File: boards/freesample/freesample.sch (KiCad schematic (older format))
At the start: 5 parts, among them J1 SMA, J2 CONN_3_PWROUT

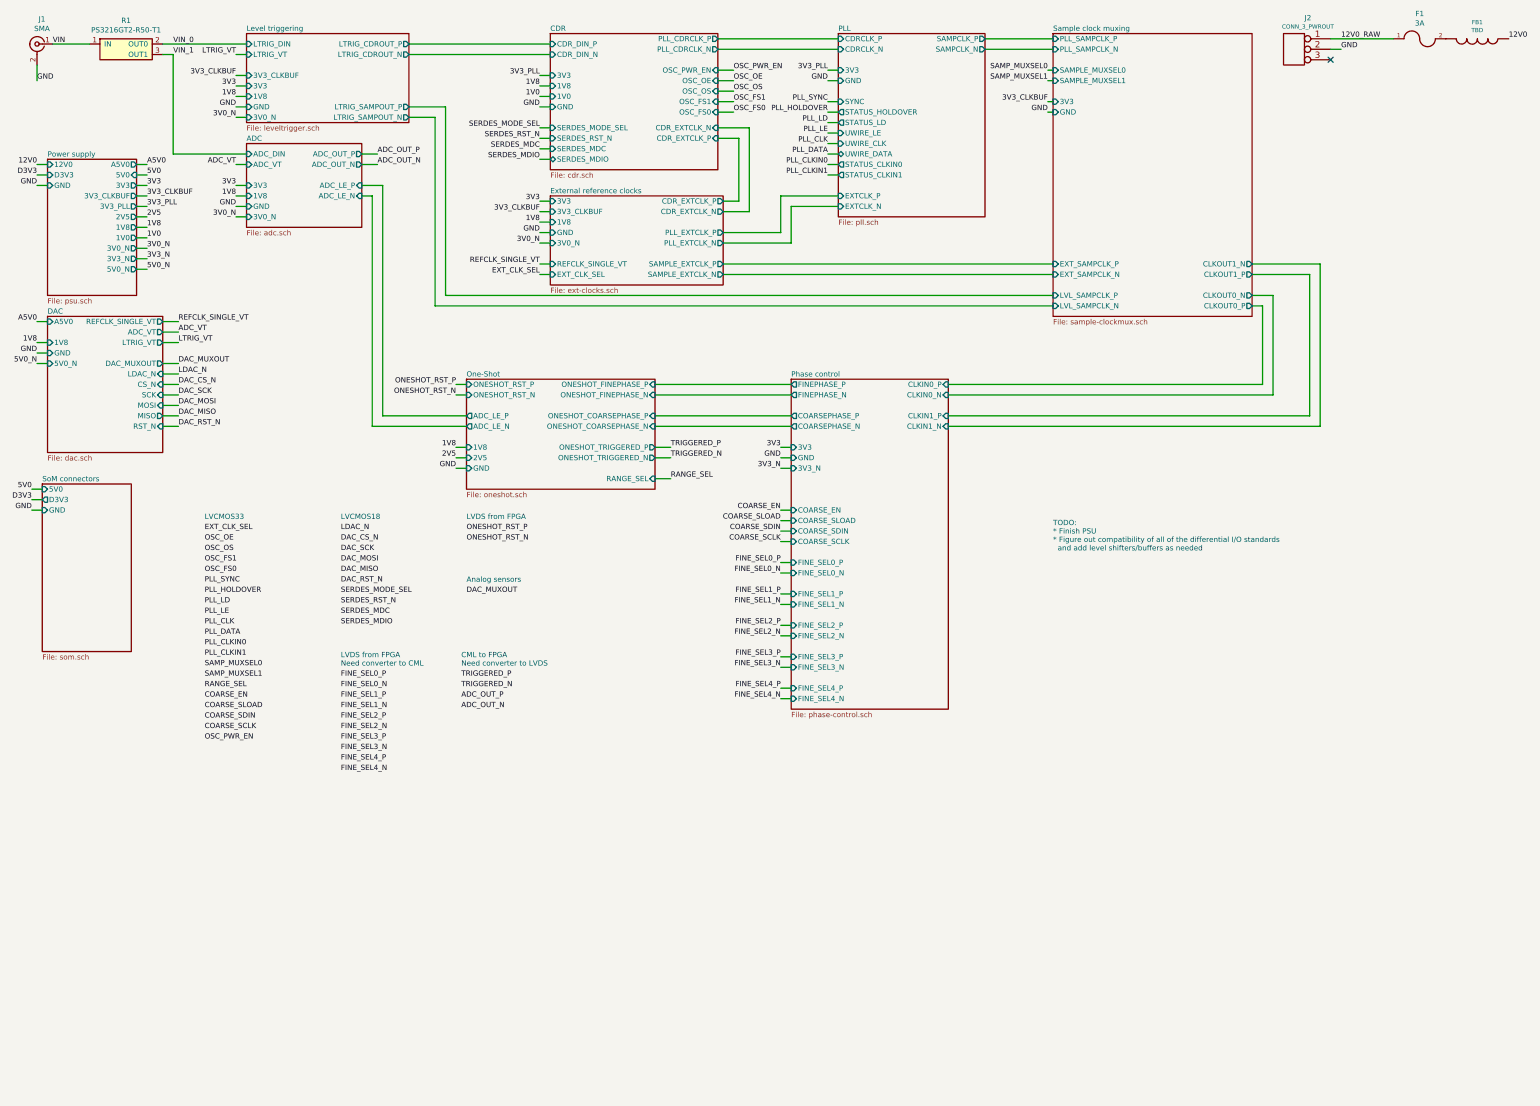
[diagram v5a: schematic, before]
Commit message: Continued schematic capture work. Hooked up most SoM connectors.
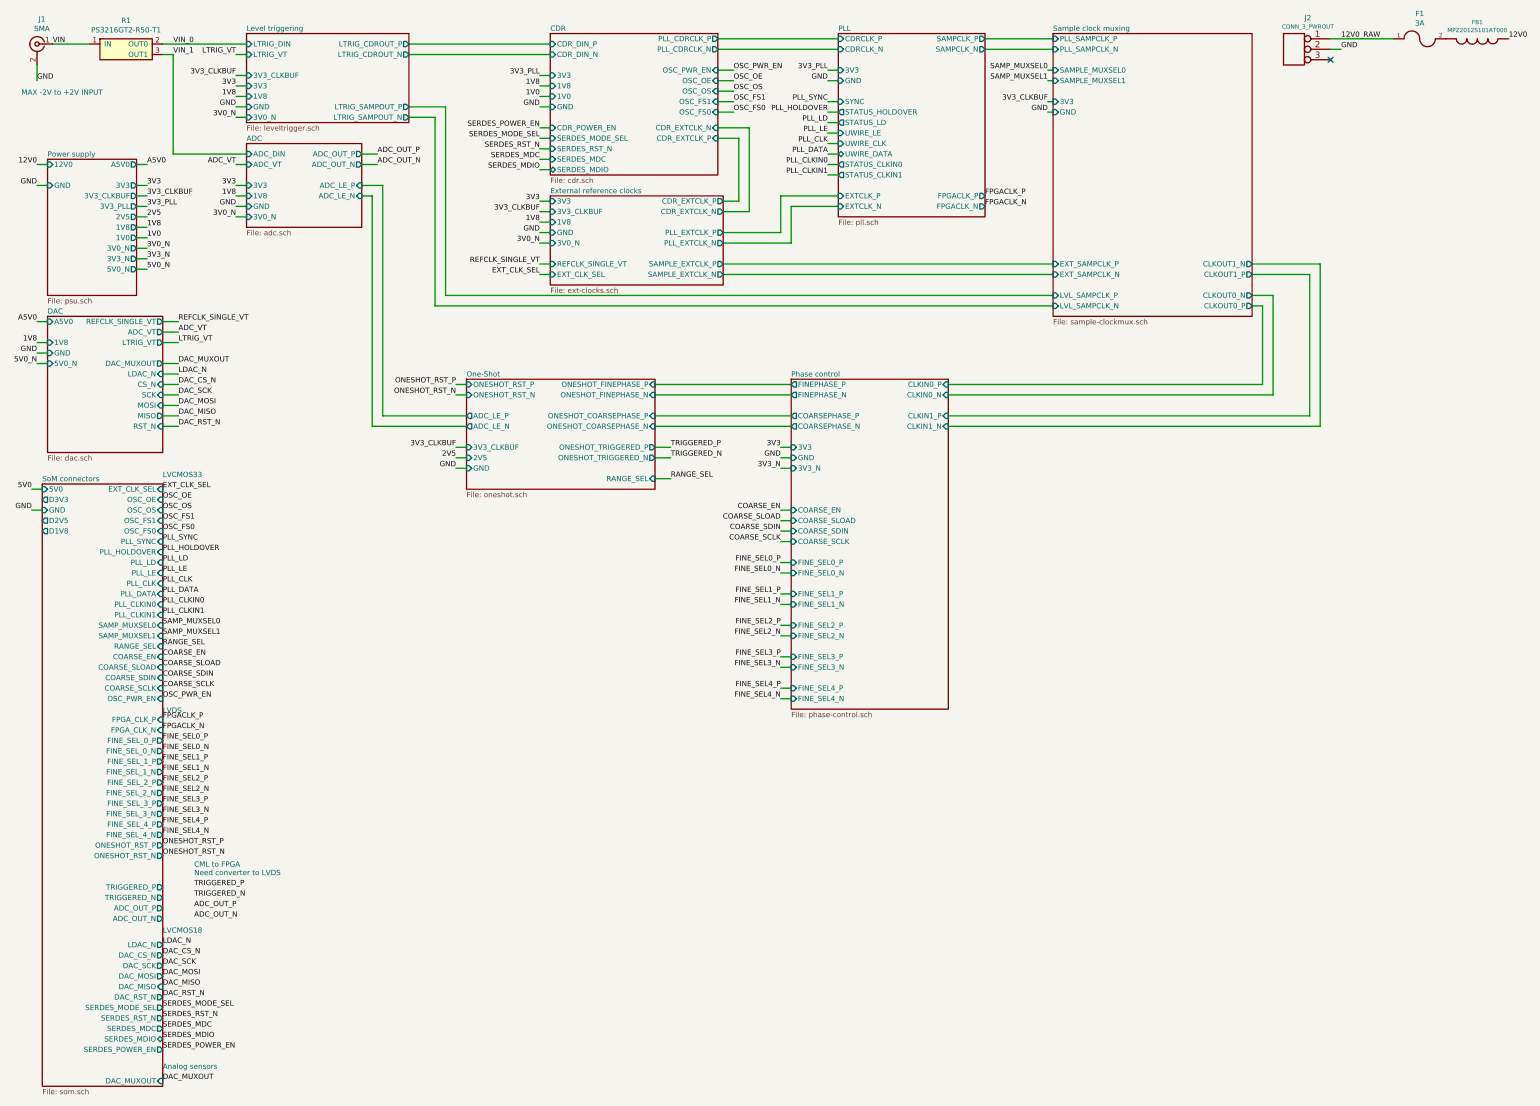
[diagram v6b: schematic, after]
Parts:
- FB1: value TBD -> MPZ2012S101AT000
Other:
- note added: "LVDS"
- note added: "MAX -2V to +2V INPUT"
- note removed: "LVDS from FPGA"
- note removed: "LVDS from FPGA\nNeed converter to CML"
- note removed: "TODO:\n* Finish PSU\n* Figure out compatibility of all of the differential I/O standards\n and add level shifters/buffers as needed"

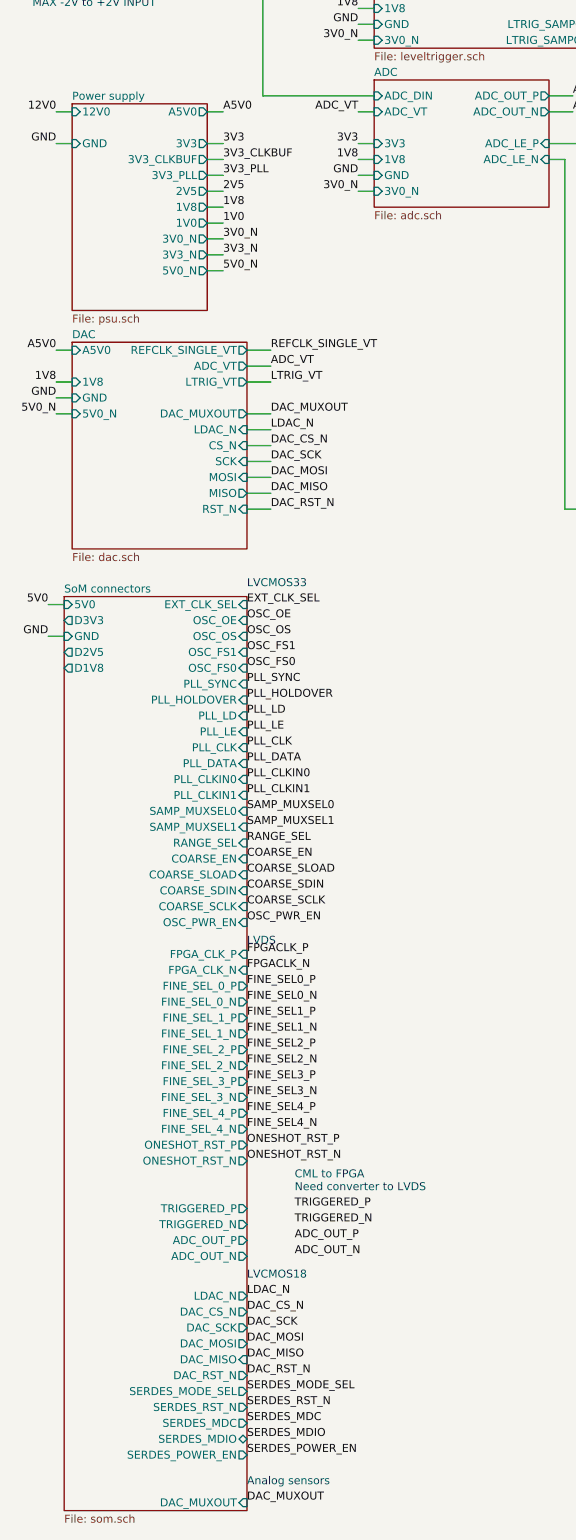
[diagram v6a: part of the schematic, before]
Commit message: Lots of ERC fixes, added CML-to-LVDS buffers for FPGA input signals
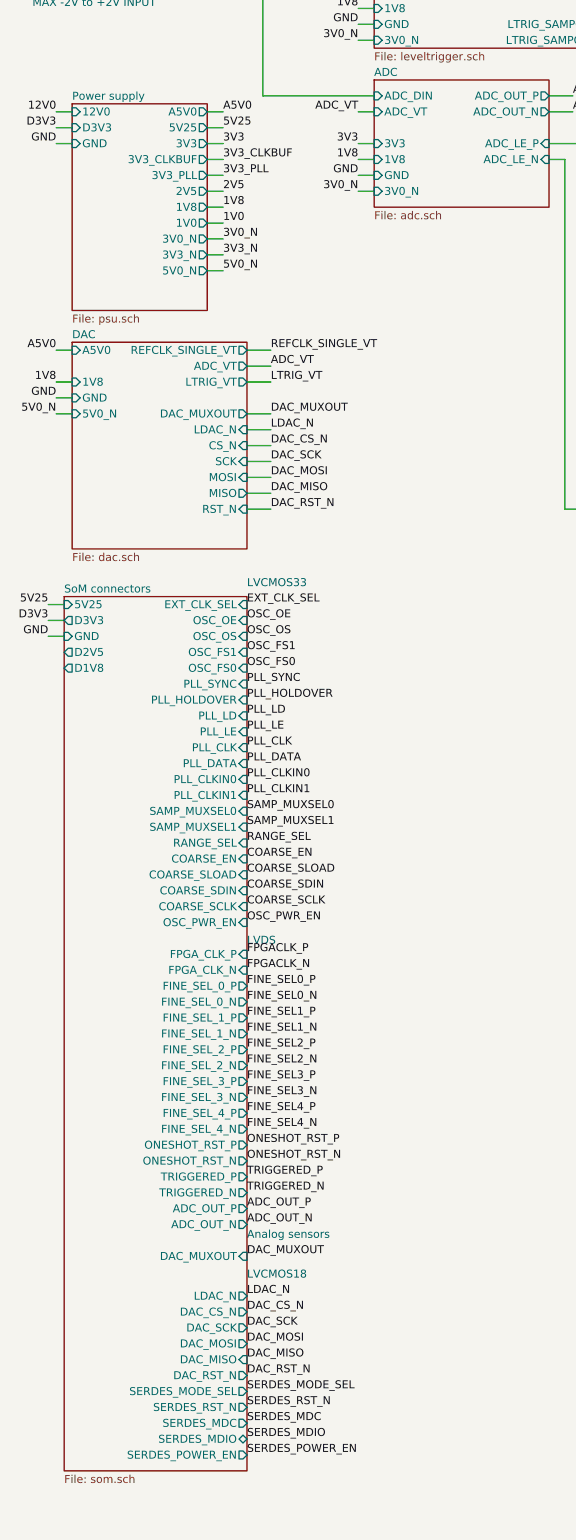
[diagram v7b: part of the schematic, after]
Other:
- note removed: "CML to FPGA\nNeed converter to LVDS"
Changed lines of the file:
@@
 	2650 950  2750 950
 $Sheet
-S 800  5050 1150 5750
+S 800  5050 1150 5500
 U 5C24BB3B
 F0 "SoM connectors" 50
 F1 "som.sch" 50
-F2 "5V0" I L 800 5100 50
-F3 "GND" I L 800 5300 50
-F4 "D3V3" O L 800 5200 50
-F5 "D2V5" O L 800 5400 50
-F6 "D1V8" O L 800 5500 50
-F7 "EXT_CLK_SEL" I R 1950 5100 50
-F8 "OSC_OE" I R 1950 5200 50
-F9 "OSC_OS" I R 1950 5300 50
-F10 "OSC_FS1" I R 1950 5400 50
-F11 "OSC_FS0" I R 1950 5500 50
-F12 "PLL_SYNC" I R 1950 5600 50
-F13 "PLL_HOLDOVER" I R 1950 5700 50
-F14 "PLL_LD" I R 1950 5800 50
-F15 "PLL_LE" I R 1950 5900 50
-F16 "PLL_CLK" I R 1950 6000 50
-F17 "PLL_DATA" I R 1950 6100 50
-F18 "PLL_CLKIN0" I R 1950 6200 50
-F19 "PLL_CLKIN1" I R 1950 6300 50
-F20 "SAMP_MUXSEL0" I R 1950 6400 50
-F21 "SAMP_MUXSEL1" I R 1950 6500 50
-F22 "RANGE_SEL" I R 1950 6600 50
-F23 "COARSE_EN" I R 1950 6700 50
-F24 "COARSE_SLOAD" I R 1950 6800 50
-F25 "COARSE_SDIN" I R 1950 6900 50
-F26 "COARSE_SCLK" I R 1950 7000 50
-F27 "OSC_PWR_EN" I R 1950 7100 50
-F28 "FPGA_CLK_P" I R 1950 7300 50
-F29 "FPGA_CLK_N" I R 1950 7400 50
-F30 "FINE_SEL_0_P" O R 1950 7500 50
-F31 "FINE_SEL_0_N" O R 1950 7600 50
-F32 "FINE_SEL_1_P" O R 1950 7700 50
-F33 "FINE_SEL_1_N" O R 1950 7800 50
-F34 "FINE_SEL_2_P" O R 1950 7900 50
-F35 "FINE_SEL_2_N" O R 1950 8000 50
-F36 "FINE_SEL_3_P" O R 1950 8100 50
-F37 "FINE_SEL_3_N" O R 1950 8200 50
-F38 "FINE_SEL_4_P" O R 1950 8300 50
-F39 "FINE_SEL_4_N" O R 1950 8400 50
-F40 "ONESHOT_RST_P" O R 1950 8500 50
-F41 "ONESHOT_RST_N" O R 1950 8600 50
-F42 "ADC_OUT_P" O R 1950 9100 50
-F43 "ADC_OUT_N" O R 1950 9200 50
-F44 "TRIGGERED_P" O R 1950 8900 50
-F45 "TRIGGERED_N" O R 1950 9000 50
-F46 "LDAC_N" O R 1950 9450 50
-F47 "DAC_CS_N" O R 1950 9550 50
-F48 "DAC_SCK" O R 1950 9650 50
-F49 "DAC_MOSI" O R 1950 9750 50
-F50 "DAC_MISO" I R 1950 9850 50
-F51 "DAC_RST_N" O R 1950 9950 50
-F52 "SERDES_MODE_SEL" O R 1950 10050 50
-F53 "SERDES_RST_N" O R 1950 10150 50
-F54 "SERDES_MDC" O R 1950 10250 50
-F55 "SERDES_MDIO" B R 1950 10350 50
-F56 "DAC_MUXOUT" I R 1950 10750 50
-F57 "SERDES_POWER_EN" O R 1950 10450 50
+F2 "GND" I L 800 5300 50
+F3 "D3V3" O L 800 5200 50
+F4 "D2V5" O L 800 5400 50
+F5 "D1V8" O L 800 5500 50
+F6 "EXT_CLK_SEL" I R 1950 5100 50
+F7 "OSC_OE" I R 1950 5200 50
+F8 "OSC_OS" I R 1950 5300 50
+F9 "OSC_FS1" I R 1950 5400 50
+F10 "OSC_FS0" I R 1950 5500 50
+F11 "PLL_SYNC" I R 1950 5600 50
+F12 "PLL_HOLDOVER" I R 1950 5700 50
+F13 "PLL_LD" I R 1950 5800 50
+F14 "PLL_LE" I R 1950 5900 50
+F15 "PLL_CLK" I R 1950 6000 50
+F16 "PLL_DATA" I R 1950 6100 50
+F17 "PLL_CLKIN0" I R 1950 6200 50
+F18 "PLL_CLKIN1" I R 1950 6300 50
+F19 "SAMP_MUXSEL0" I R 1950 6400 50
+F20 "SAMP_MUXSEL1" I R 1950 6500 50
+F21 "RANGE_SEL" I R 1950 6600 50
+F22 "COARSE_EN" I R 1950 6700 50
+F23 "COARSE_SLOAD" I R 1950 6800 50
+F24 "COARSE_SDIN" I R 1950 6900 50
+F25 "COARSE_SCLK" I R 1950 7000 50
+F26 "OSC_PWR_EN" I R 1950 7100 50
+F27 "FPGA_CLK_P" I R 1950 7300 50
+F28 "FPGA_CLK_N" I R 1950 7400 50
+F29 "FINE_SEL_0_P" O R 1950 7500 50
+F30 "FINE_SEL_0_N" O R 1950 7600 50
+F31 "FINE_SEL_1_P" O R 1950 7700 50
+F32 "FINE_SEL_1_N" O R 1950 7800 50
+F33 "FINE_SEL_2_P" O R 1950 7900 50
+F34 "FINE_SEL_2_N" O R 1950 8000 50
+F35 "FINE_SEL_3_P" O R 1950 8100 50
+F36 "FINE_SEL_3_N" O R 1950 8200 50
+F37 "FINE_SEL_4_P" O R 1950 8300 50
+F38 "FINE_SEL_4_N" O R 1950 8400 50
+F39 "ONESHOT_RST_P" O R 1950 8500 50
+F40 "ONESHOT_RST_N" O R 1950 8600 50
+F41 "ADC_OUT_P" O R 1950 8900 50
+F42 "ADC_OUT_N" O R 1950 9000 50
+F43 "TRIGGERED_P" O R 1950 8700 50
+F44 "TRIGGERED_N" O R 1950 8800 50
+F45 "LDAC_N" O R 1950 9450 50
+F46 "DAC_CS_N" O R 1950 9550 50
+F47 "DAC_SCK" O R 1950 9650 50
+F48 "DAC_MOSI" O R 1950 9750 50
+F49 "DAC_MISO" I R 1950 9850 50
+F50 "DAC_RST_N" O R 1950 9950 50
+F51 "SERDES_MODE_SEL" O R 1950 10050 50
+F52 "SERDES_RST_N" O R 1950 10150 50
+F53 "SERDES_MDC" O R 1950 10250 50
+F54 "SERDES_MDIO" B R 1950 10350 50
+F55 "DAC_MUXOUT" I R 1950 9200 50
+F56 "SERDES_POWER_EN" O R 1950 10450 50
+F57 "5V25" I L 800 5100 50
 $EndSheet
 $Sheet
@@
 F0 "Power supply" 50
 F1 "psu.sch" 50
-F3 "3V3" O R 1700 2200 50
-F4 "3V0_N" O R 1700 2800 50
-F5 "1V8" O R 1700 2600 50
-F6 "GND" I L 850 2200 50
-F7 "1V0" O R 1700 2700 50
-F8 "5V0_N" O R 1700 3000 50
-F9 "12V0" I L 850 2000 50
-F10 "3V3_N" O R 1700 2900 50
-F11 "2V5" O R 1700 2500 50
-F12 "A5V0" O R 1700 2000 50
-F14 "3V3_PLL" O R 1700 2400 50
-F15 "3V3_CLKBUF" O R 1700 2300 50
+F2 "3V3" O R 1700 2200 50
+F3 "3V0_N" O R 1700 2800 50
+F4 "1V8" O R 1700 2600 50
+F5 "GND" I L 850 2200 50
+F6 "1V0" O R 1700 2700 50
+F7 "5V0_N" O R 1700 3000 50
+F8 "12V0" I L 850 2000 50
+F9 "3V3_N" O R 1700 2900 50
+F10 "2V5" O R 1700 2500 50
+F11 "A5V0" O R 1700 2000 50
+F12 "3V3_PLL" O R 1700 2400 50
+F13 "3V3_CLKBUF" O R 1700 2300 50
+F14 "5V25" O R 1700 2100 50
+F15 "D3V3" I L 850 2100 50
 $EndSheet
 Text Label 8300 1100 2    50   ~ 0
@@
 Wire Wire Line
 	6800 4800 6650 4800
-Text Label 2250 8900 0    50   ~ 0
+Text Label 1950 8700 0    50   ~ 0
 TRIGGERED_P
-Text Label 2250 9000 0    50   ~ 0
+Text Label 1950 8800 0    50   ~ 0
 TRIGGERED_N
-Text Label 2250 9100 0    50   ~ 0
+Text Label 1950 8900 0    50   ~ 0
 ADC_OUT_P
-Text Label 2250 9200 0    50   ~ 0
+Text Label 1950 9000 0    50   ~ 0
 ADC_OUT_N
 Text Label 1950 5100 0    50   ~ 0
@@
 Wire Wire Line
 	9800 900  10450 900
-Text Label 1950 10750 0    50   ~ 0
+Text Label 1950 9200 0    50   ~ 0
 DAC_MUXOUT
 Text Label 1950 9450 0    50   ~ 0
@@
 Text Label 1950 8400 0    50   ~ 0
 FINE_SEL4_N
-Text Notes 2250 8800 0    50   ~ 0
-CML to FPGA\nNeed converter to LVDS
 Text Notes 1950 5000 0    50   ~ 0
 LVCMOS33
-Text Notes 1950 10650 0    50   ~ 0
+Text Notes 1950 9100 0    50   ~ 0
 Analog sensors
 Text Label 750  3700 2    50   ~ 0
@@
 	1800 2000 1700 2000
 Text Label 700  5100 2    50   ~ 0
-5V0
+5V25
 Wire Wire Line
 	700  5100 800  5100
@@
 Wire Wire Line
 	4750 4700 4850 4700
+Text Label 1800 2100 0    50   ~ 0
+5V25
+Wire Wire Line
+	1800 2100 1700 2100
+Text Label 700  5200 2    50   ~ 0
+D3V3
+Wire Wire Line
+	700  5200 800  5200
+Text Label 750  2100 2    50   ~ 0
+D3V3
+Wire Wire Line
+	750  2100 850  2100
 $EndSCHEMATC

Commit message: Finished PSU schematic. Ready for design review!
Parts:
- added J11, J12: SMA, symbol Connector:Conn_Coaxial
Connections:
- net GND: now also J11.2 (Ext), J12.2 (Ext)
- new net One-Shot/CLKOUT_N: J12.1 (In)
- new net One-Shot/CLKOUT_P: J11.1 (In)
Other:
- note added: "Phase shifted sampling clock out\nfor debugging or external logic"
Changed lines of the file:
@@
 Sheet 1 12
 Title "FREESAMPLE Oscilloscope"
-Date "2019-03-10"
+Date "2019-03-11"
 Rev "0.1"
 Comp "Andrew D. Zonenberg / Antikernel Labs"
@@
 $EndSheet
 $Sheet
-S 4850 4050 1800 1050
+S 4850 4050 1800 1400
 U 5C15809A
 F0 "One-Shot" 50
@@
 F14 "2V5" I L 4850 4800 50
 F15 "3V3_CLKBUF" I L 4850 4700 50
+F16 "CLKOUT_P" I L 4850 5050 50
+F17 "CLKOUT_N" I L 4850 5200 50
 $EndSheet
 $Comp
@@
 Wire Wire Line
 	750  2100 850  2100
+$Comp
+L Connector:Conn_Coaxial J12
+U 1 1 5D23CAB3
+P 4100 5200
+F 0 "J12" H 4000 5000 50  0000 C CNN
+F 1 "SMA" H 4000 5100 50  0000 C CNN
+F 2 "" H 4100 5200 50  0001 C CNN
+F 3 "" H 4100 5200 50  0001 C CNN
+	1    4100 5200
+	-1   0    0    -1
+$EndComp
+$Comp
+L Connector:Conn_Coaxial J11
+U 1 1 5D23D75B
+P 4100 5050
+F 0 "J11" H 4000 4850 50  0000 C CNN
+F 1 "SMA" H 4000 4950 50  0000 C CNN
+F 2 "" H 4100 5050 50  0001 C CNN
+F 3 "" H 4100 5050 50  0001 C CNN
+	1    4100 5050
+	-1   0    0    1
+$EndComp
+Wire Wire Line
+	4850 5200 4250 5200
+Text Label 4100 4850 2    50   ~ 0
+GND
+Text Label 4100 5400 2    50   ~ 0
+GND
+Wire Wire Line
+	4250 5050 4850 5050
+Text Notes 4100 5750 0    50   ~ 0
+Phase shifted sampling clock out\nfor debugging or external logic
 $EndSCHEMATC
